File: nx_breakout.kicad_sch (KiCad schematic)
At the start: 19 parts, among them J1 Conn_02x20_Odd_Even, J2 Conn_01x06, J3 Conn_01x04, J4 Conn_01x04, J5 Conn_01x04_Male, U1 SN74LVC1G14DBV, U2 SN74LVC1G14DBV, U3 SN74LVC1G14DBV, U4 SN74LVC1G14DBV, U5 SN74LVC1G14DBV

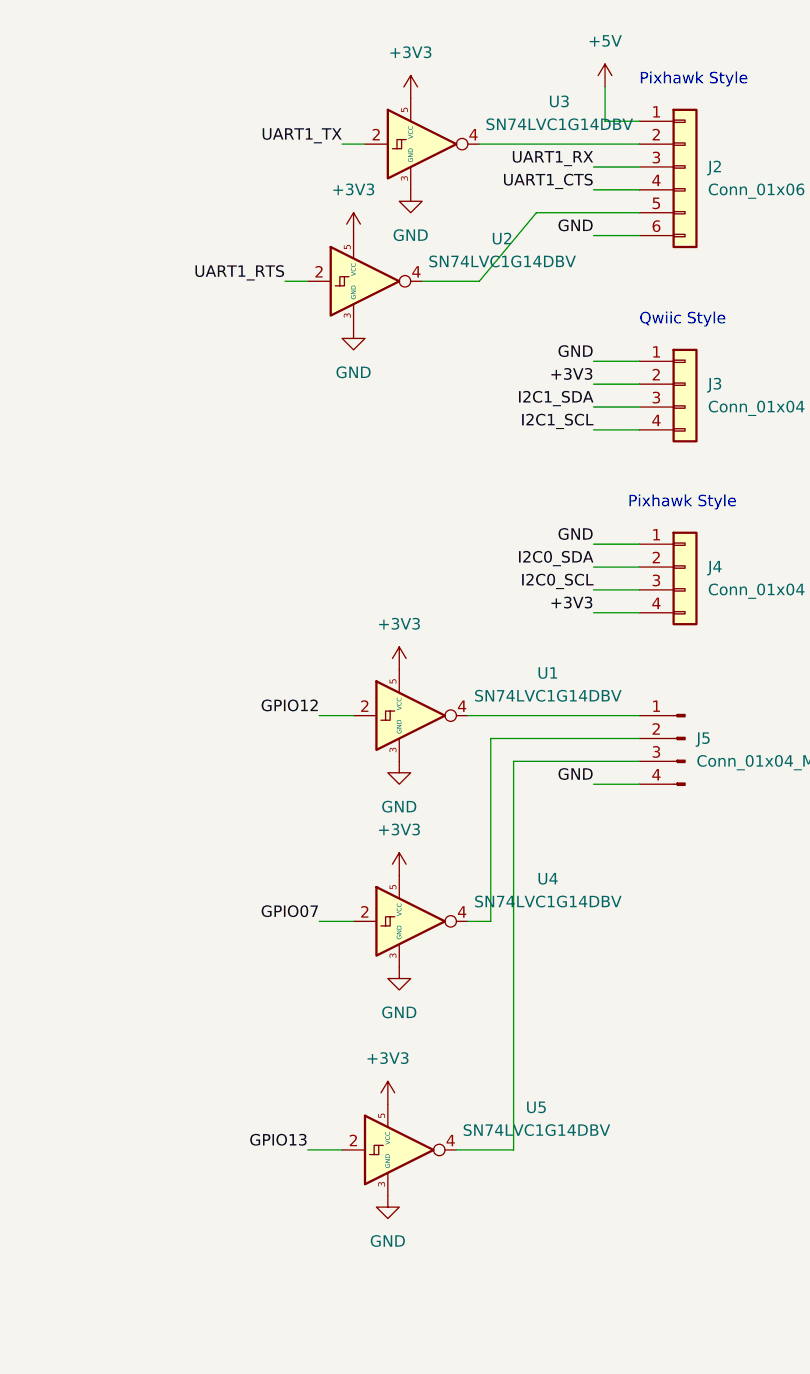
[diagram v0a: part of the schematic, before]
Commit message: Add files via upload
Corrected to non-inverting Schmitt triggers.
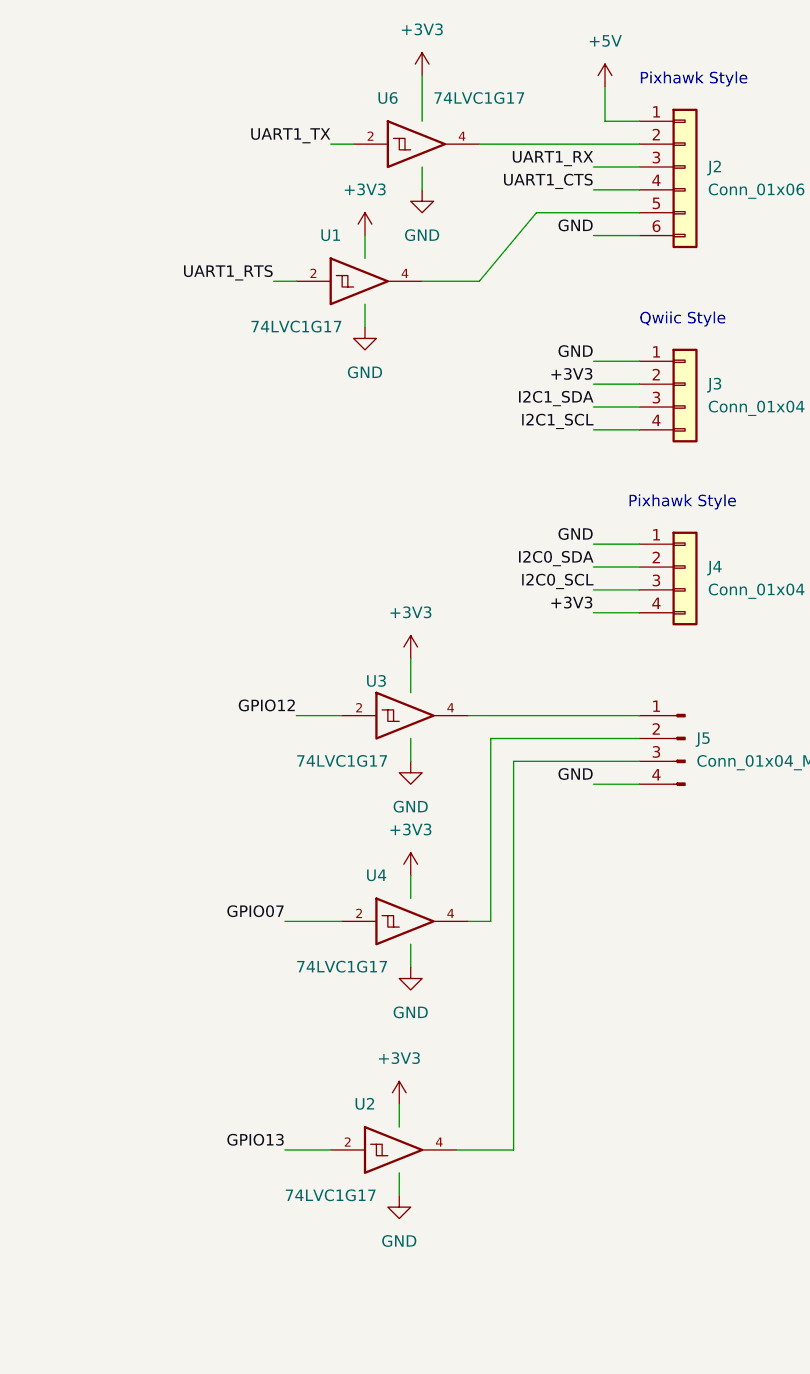
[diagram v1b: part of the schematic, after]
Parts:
- removed U1, U2, U3, U4, U5: SN74LVC1G14DBV, Package_TO_SOT_SMD:SOT-23-5, symbol 74xGxx:SN74LVC1G14DBV
- added U1, U2, U3, U4, U6: 74LVC1G17, Package_TO_SOT_SMD:SOT-23-5_HandSoldering, symbol 74xGxx:74LVC1G17
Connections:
- net +3V3: now also U1.5 (VCC), U2.5 (VCC), U3.5 (VCC), U4.5 (VCC), U6.5 (VCC)
- net GND: now also U1.3 (GND), U2.3 (GND), U3.3 (GND), U4.3 (GND), U6.3 (GND)
- net GPIO07: now also U4.2
- net GPIO12: now also U3.2
- net GPIO13: now also U2.2
- net UART1_RTS: now also U1.2
- net UART1_TX: now also U6.2
- net at J5.1 (Pin_1): now also U3.4
- net at J5.2 (Pin_2): now also U4.4
- net at J5.3 (Pin_3): now also U2.4
- net at J2.5 (Pin_5): now also U1.4
- net at J2.2 (Pin_2): now also U6.4
